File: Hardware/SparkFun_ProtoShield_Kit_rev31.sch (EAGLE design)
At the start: 29 parts

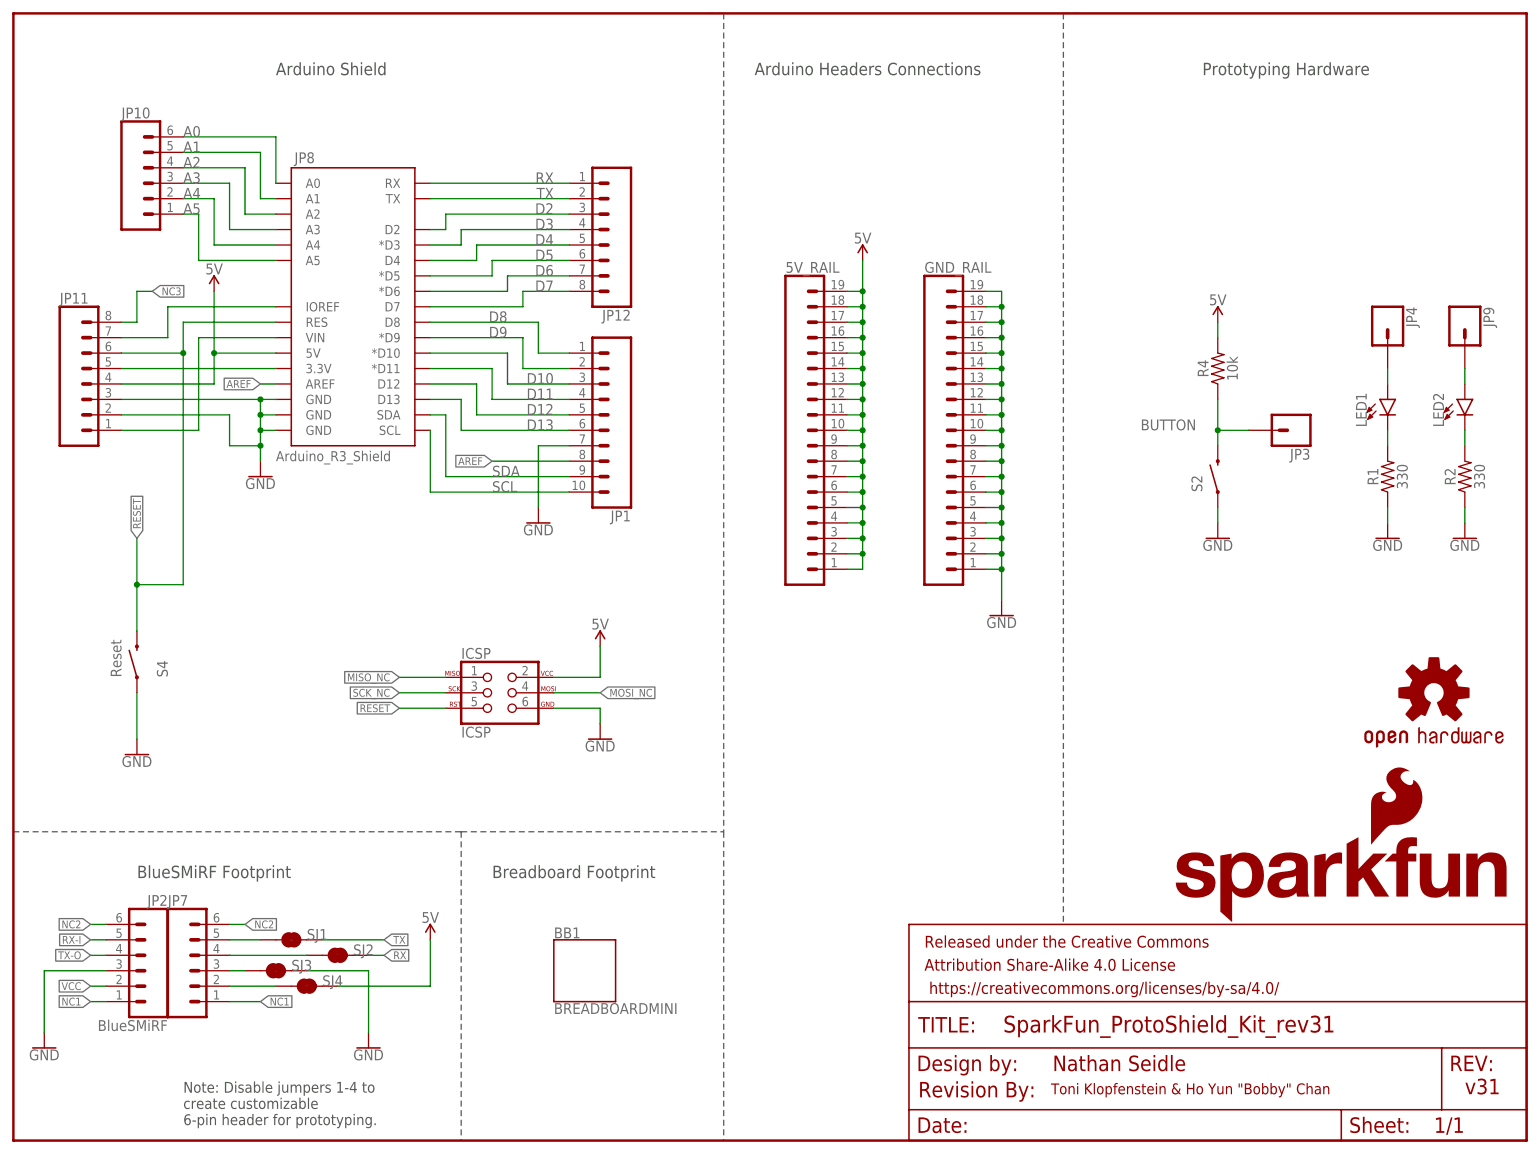
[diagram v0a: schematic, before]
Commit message: Add files via upload
**Board**

* Change wire boundary to bRestrict layer to prevent ground pour from creating a thermal around GND jumper pads.

**Schematic**

* Move OSHW logo next to SparkFun logo
* Move schematic components around to make use of the empty space
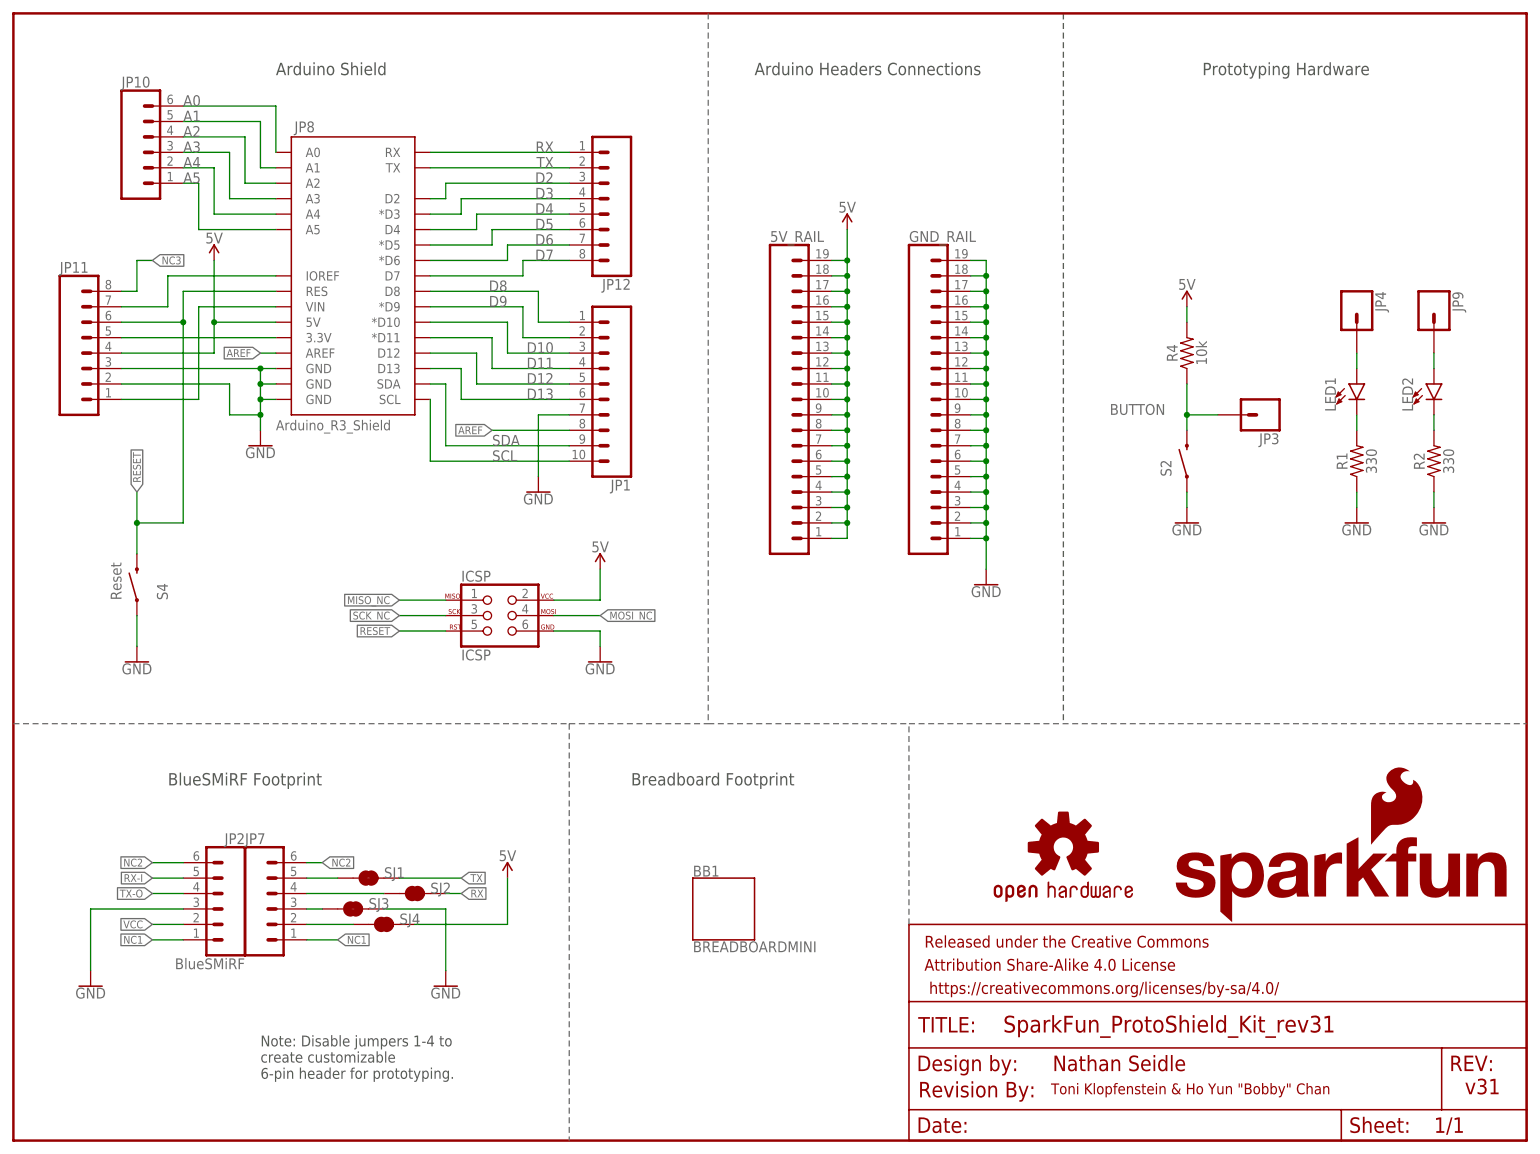
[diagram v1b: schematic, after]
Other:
- moved on the sheet: 5V_RAIL, BB1, GND_RAIL, ICSP, JP1, JP10, JP11, JP12, JP2, JP3, JP4, JP7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
